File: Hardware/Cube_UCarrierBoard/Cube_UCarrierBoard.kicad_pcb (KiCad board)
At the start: 2 copper layers, 1 part

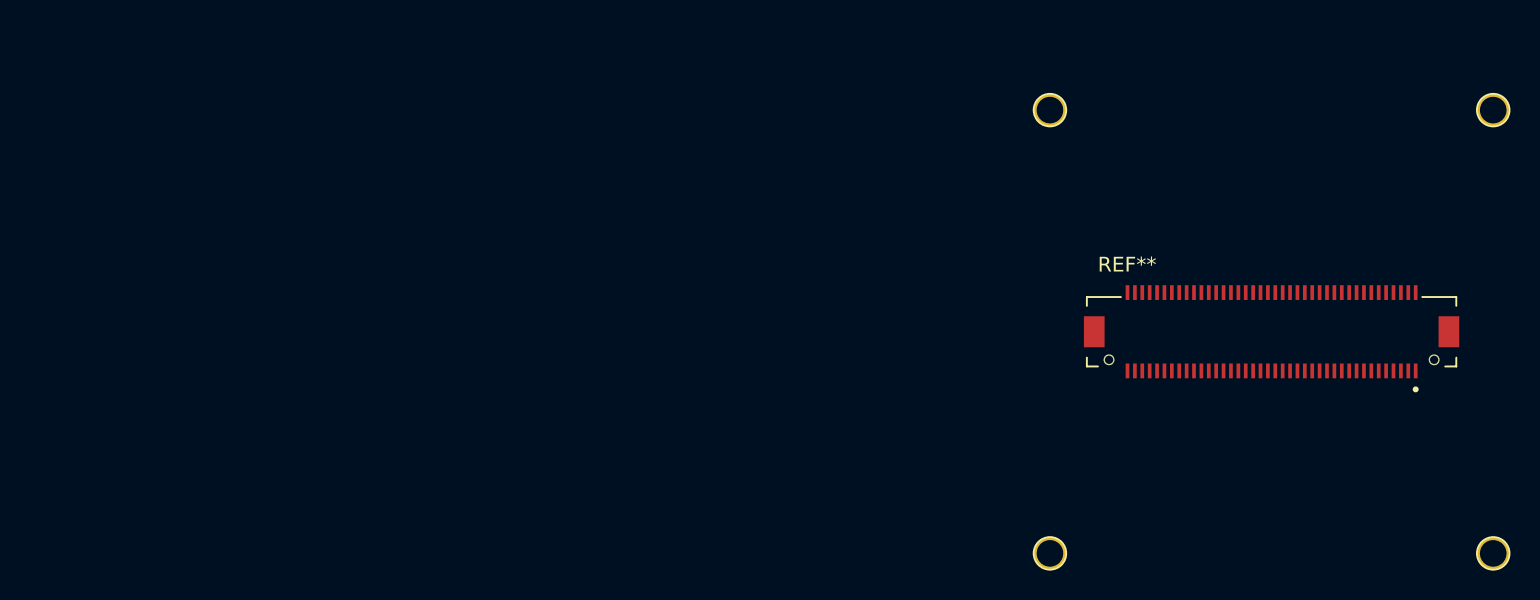
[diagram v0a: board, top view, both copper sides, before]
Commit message: Footprints & Symbols for JST & Molex connectors
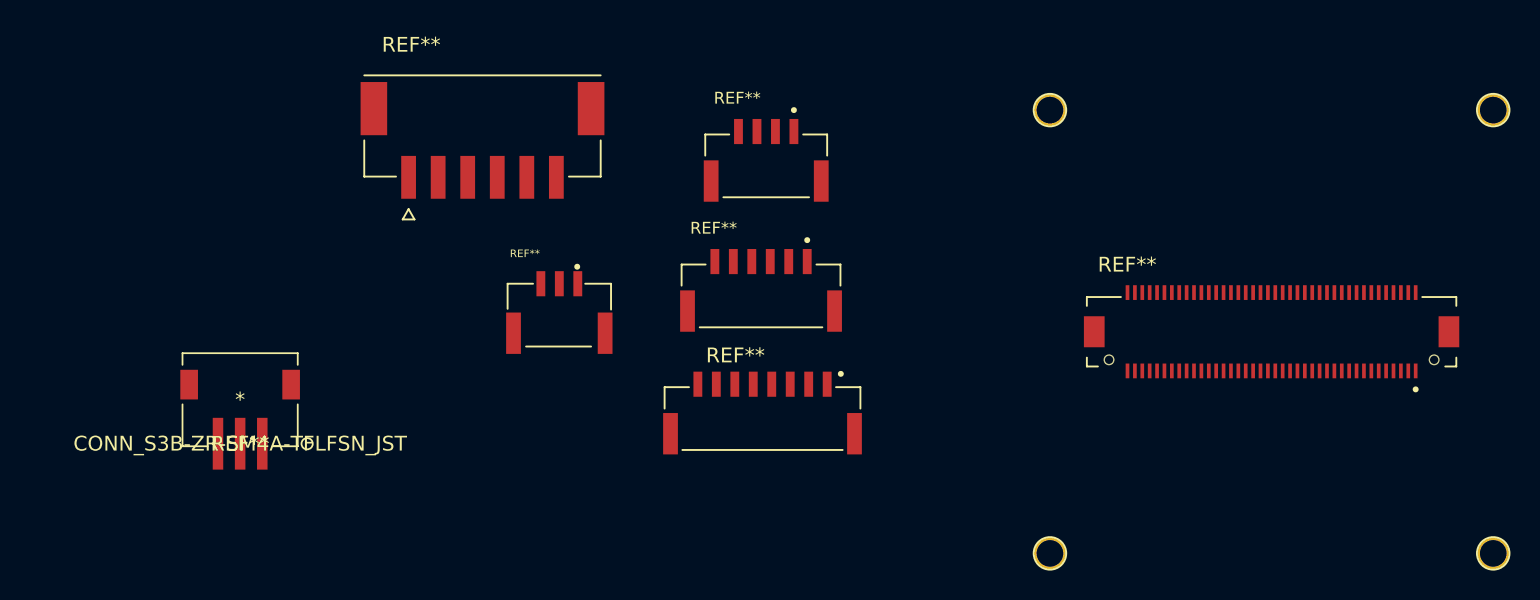
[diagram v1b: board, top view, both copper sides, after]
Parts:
- added REF**: CONN_S3B-ZR-SM4A-TFLFSN_JST, libraries:S3B-ZR-SM4A-TFLFSN, F.Cu at (75.7, 105.3)
- added REF**: MOLEX_5024430670, libraries:MOLEX_5024430670, F.Cu at (92.0, 87.2)
- added REF**: JST_BM08B-GHS-TBT_LF__SN__N_, libraries:JST_BM08B-GHS-TBT(LF)(SN)(N), F.Cu at (111.0, 104.3)
- added REF**: CONN_BM03B-GHS-TBT_LF__SN__N_, libraries:CONN_BM03B-GHS-TBT(LF)(SN)(N), F.Cu at (97.2, 97.5)
- added REF**: JST_BM04B-GHS-TBT_LF__SN__N_, libraries:JST_BM04B-GHS-TBT(LF)(SN)(N), F.Cu at (111.2, 90.5)
- added REF**: JST_BM06B-GHS-TBT_LF__SN__N_, libraries:JST_BM06B-GHS-TBT(LF)(SN)(N), F.Cu at (110.9, 99.3)
